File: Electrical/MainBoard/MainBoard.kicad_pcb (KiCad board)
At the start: 4 copper layers, 0 parts

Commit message: Add the majority of the electronics
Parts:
- added C1: 0.1 uF, Capacitor_SMD:C_0805_2012Metric_Pad1.18x1.45mm_HandSolder, F.Cu at (238.4, 136.1)
- added C10: 0.1 uF, Capacitor_SMD:C_0805_2012Metric_Pad1.18x1.45mm_HandSolder, F.Cu at (243.2, 148.1)
- added C11: 4.7 uF, Capacitor_SMD:C_0805_2012Metric_Pad1.18x1.45mm_HandSolder, F.Cu at (203.9, 170.2)
- added C12: 4.7 uF, Capacitor_SMD:C_0805_2012Metric_Pad1.18x1.45mm_HandSolder, F.Cu at (203.9, 173.2)
- added C13: 10 uF, Capacitor_THT:CP_Radial_Tantal_D5.0mm_P2.50mm, F.Cu at (197.0, 172.0)
- added C14: 0.1 uF, Capacitor_SMD:C_0805_2012Metric_Pad1.18x1.45mm_HandSolder, F.Cu at (204.2, 103.0)
- added C15: 2.2 uF, Capacitor_SMD:C_0805_2012Metric_Pad1.18x1.45mm_HandSolder, F.Cu at (204.2, 106.0)
- added C16: 10 nF, Capacitor_SMD:C_0805_2012Metric_Pad1.18x1.45mm_HandSolder, F.Cu at (204.2, 109.0)
- added C17: 0.1 uF, Capacitor_SMD:C_0805_2012Metric_Pad1.18x1.45mm_HandSolder, F.Cu at (192.0, 98.0)
- added C18: 4.7 uF, Capacitor_SMD:C_0805_2012Metric_Pad1.18x1.45mm_HandSolder, F.Cu at (267.4, 143.5)
- added C19: 4.7 uF, Capacitor_SMD:C_0805_2012Metric_Pad1.18x1.45mm_HandSolder, F.Cu at (267.4, 146.5)
- added C2: 0.1 uF, Capacitor_SMD:C_0805_2012Metric_Pad1.18x1.45mm_HandSolder, F.Cu at (238.4, 139.1)
- added C3: 0.1 uF, Capacitor_SMD:C_0805_2012Metric_Pad1.18x1.45mm_HandSolder, F.Cu at (238.4, 142.1)
- added C4: 0.1 uF, Capacitor_SMD:C_0805_2012Metric_Pad1.18x1.45mm_HandSolder, F.Cu at (238.4, 145.1)
- added C5: 0.1 uF, Capacitor_SMD:C_0805_2012Metric_Pad1.18x1.45mm_HandSolder, F.Cu at (238.4, 148.1)
- added C6: 0.1 uF, Capacitor_SMD:C_0805_2012Metric_Pad1.18x1.45mm_HandSolder, F.Cu at (243.2, 136.1)
- added C7: 0.1 uF, Capacitor_SMD:C_0805_2012Metric_Pad1.18x1.45mm_HandSolder, F.Cu at (243.2, 139.1)
- added C8: 0.1 uF, Capacitor_SMD:C_0805_2012Metric_Pad1.18x1.45mm_HandSolder, F.Cu at (243.2, 142.1)
- added C9: 0.1 uF, Capacitor_SMD:C_0805_2012Metric_Pad1.18x1.45mm_HandSolder, F.Cu at (243.2, 145.1)
- added D1: LED 2, LED_SMD:LED_0805_2012Metric_Pad1.15x1.40mm_HandSolder, F.Cu at (197.3, 150.0)
- added D2: LED 1, LED_SMD:LED_0805_2012Metric_Pad1.15x1.40mm_HandSolder, F.Cu at (197.3, 153.0)
- added D3: LED 4, LED_SMD:LED_0805_2012Metric_Pad1.15x1.40mm_HandSolder, F.Cu at (197.3, 156.1)
- added D4: LED 3, LED_SMD:LED_0805_2012Metric_Pad1.15x1.40mm_HandSolder, F.Cu at (197.3, 159.1)
- added D5: LED 6, LED_SMD:LED_0805_2012Metric_Pad1.15x1.40mm_HandSolder, F.Cu at (197.3, 162.2)
- added D6: LED 5, LED_SMD:LED_0805_2012Metric_Pad1.15x1.40mm_HandSolder, F.Cu at (197.3, 165.2)
- added D7: ON, LED_SMD:LED_0805_2012Metric_Pad1.15x1.40mm_HandSolder, F.Cu at (203.9, 176.3)
- added D8: Status_LED, RobotLibrary:CONN3_22232031_MOL, F.Cu at (192.7, 105.4)
- added F1: 5A Fuse, RobotLibrary:FUSE_4628, F.Cu at (228.3, 75.0)
- added H1: MountingHole, MountingHole:MountingHole_3.2mm_M3, F.Cu at (169.2, 86.0)
- added H2: MountingHole, MountingHole:MountingHole_3.2mm_M3, F.Cu at (261.7, 86.0)
- added H3: MountingHole, MountingHole:MountingHole_3.2mm_M3, F.Cu at (169.3, 178.5)
- added H4: MountingHole, MountingHole:MountingHole_3.2mm_M3, F.Cu at (261.7, 178.5)
- added J1: SNAP Program, Connector_PinSocket_2.54mm:PinSocket_1x06_P2.54mm_Horizontal, F.Cu at (247.0, 116.6)
- added J10: Refl_Mount, Connector_PinHeader_2.54mm:PinHeader_2x02_P2.54mm_Vertical, F.Cu at (250.2, 196.1)
- added J11: Refl_Mount, Connector_PinHeader_2.54mm:PinHeader_2x02_P2.54mm_Vertical, F.Cu at (250.2, 203.3)
- added J12: Refl_PCB_Connect, RobotLibrary:CONN3_22232031_MOL, F.Cu at (255.6, 96.7)
- added J13: Refl_PCB_Connect, RobotLibrary:CONN3_22232031_MOL, F.Cu at (255.6, 104.7)
- added J14: Refl_PCB_Connect, RobotLibrary:CONN3_22232031_MOL, F.Cu at (255.6, 112.7)
- added J2: UART Connect, Connector_PinHeader_2.54mm:PinHeader_2x06_P2.54mm_Vertical, F.Cu at (204.9, 122.6)
- added J3: SPI Connect, Connector_PinHeader_2.54mm:PinHeader_2x08_P2.54mm_Vertical, F.Cu at (197.7, 122.6)
- added J4: 5V Supply, Connector_PinHeader_2.54mm:PinHeader_2x05_P2.54mm_Vertical, F.Cu at (250.8, 155.8)
- added J5: 3.3V Supply, Connector_PinHeader_2.54mm:PinHeader_2x05_P2.54mm_Vertical, F.Cu at (258.0, 155.8)
- added J6: USB_B_Micro, RobotLibrary:AMPHENOL_10118193-0001LF, F.Cu at (217.5, 110.4)
- added J7: Battery1, RobotLibrary:CONN_1017514, F.Cu at (218.2, 86.7)
- added J8: Battery1, RobotLibrary:CONN_1017514, F.Cu at (234.8, 86.7)
- added J9: Refl_Mount, Connector_PinHeader_2.54mm:PinHeader_2x02_P2.54mm_Vertical, F.Cu at (239.8, 187.7)
- added K1: QRE1113GR, RobotLibrary:ARUSM-313_100CY_FAS-M, F.Cu at (234.6, 189.4)
- added K2: QRE1113GR, RobotLibrary:ARUSM-313_100CY_FAS-M, F.Cu at (250.7, 189.7)
- added K3: QRE1113GR, RobotLibrary:ARUSM-313_100CY_FAS-M, F.Cu at (256.5, 189.7)
- added R1: 1k, Resistor_SMD:R_0805_2012Metric_Pad1.20x1.40mm_HandSolder, F.Cu at (222.8, 144.0)
- added R10: 1k, Resistor_SMD:R_0805_2012Metric_Pad1.20x1.40mm_HandSolder, F.Cu at (190.5, 150.0)
- added R11: 1k, Resistor_SMD:R_0805_2012Metric_Pad1.20x1.40mm_HandSolder, F.Cu at (190.5, 152.9)
- added R12: 1k, Resistor_SMD:R_0805_2012Metric_Pad1.20x1.40mm_HandSolder, F.Cu at (190.5, 155.9)
- added R13: 1k, Resistor_SMD:R_0805_2012Metric_Pad1.20x1.40mm_HandSolder, F.Cu at (190.5, 158.8)
- added R14: 1k, Resistor_SMD:R_0805_2012Metric_Pad1.20x1.40mm_HandSolder, F.Cu at (185.2, 86.3)
- added R15: 1k, Resistor_SMD:R_0805_2012Metric_Pad1.20x1.40mm_HandSolder, F.Cu at (185.2, 89.2)
- added R16: 1k, Resistor_SMD:R_0805_2012Metric_Pad1.20x1.40mm_HandSolder, F.Cu at (185.2, 92.2)
- added R17: 130R, Resistor_SMD:R_0805_2012Metric_Pad1.20x1.40mm_HandSolder, F.Cu at (191.9, 111.0)
- added R18: 130R, Resistor_SMD:R_0805_2012Metric_Pad1.20x1.40mm_HandSolder, F.Cu at (191.9, 113.9)
- added R19: 100R, Resistor_SMD:R_0805_2012Metric_Pad1.20x1.40mm_HandSolder, F.Cu at (239.9, 194.1)
- added R2: 10k, Resistor_SMD:R_0805_2012Metric_Pad1.20x1.40mm_HandSolder, F.Cu at (222.8, 147.0)
- added R20: 10k, Resistor_SMD:R_0805_2012Metric_Pad1.20x1.40mm_HandSolder, F.Cu at (239.9, 197.0)
- added R21: 100R, Resistor_SMD:R_0805_2012Metric_Pad1.20x1.40mm_HandSolder, F.Cu at (257.4, 195.2)
- added R22: 10k, Resistor_SMD:R_0805_2012Metric_Pad1.20x1.40mm_HandSolder, F.Cu at (257.4, 198.2)
- added R23: 100R, Resistor_SMD:R_0805_2012Metric_Pad1.20x1.40mm_HandSolder, F.Cu at (257.4, 201.2)
- added R24: 10k, Resistor_SMD:R_0805_2012Metric_Pad1.20x1.40mm_HandSolder, F.Cu at (257.4, 204.1)
- added R3: 130R, Resistor_SMD:R_0805_2012Metric_Pad1.20x1.40mm_HandSolder, F.Cu at (202.0, 150.0)
- added R4: 130R, Resistor_SMD:R_0805_2012Metric_Pad1.20x1.40mm_HandSolder, F.Cu at (202.0, 152.9)
- added R5: 130R, Resistor_SMD:R_0805_2012Metric_Pad1.20x1.40mm_HandSolder, F.Cu at (202.0, 155.9)
- added R6: 130R, Resistor_SMD:R_0805_2012Metric_Pad1.20x1.40mm_HandSolder, F.Cu at (202.0, 158.8)
- added R7: 130R, Resistor_SMD:R_0805_2012Metric_Pad1.20x1.40mm_HandSolder, F.Cu at (202.0, 161.8)
- added R8: 130R, Resistor_SMD:R_0805_2012Metric_Pad1.20x1.40mm_HandSolder, F.Cu at (202.0, 164.7)
- added R9: 130R, Resistor_SMD:R_0805_2012Metric_Pad1.20x1.40mm_HandSolder, F.Cu at (197.2, 176.7)
- added SW1: Reset, RobotLibrary:SW_B3F-1000_OMR, F.Cu at (212.3, 145.8)
- added SW10: User_Button, RobotLibrary:CONN_22232021_MOL, F.Cu at (178.3, 104.8)
- added SW2: 5V Bypass, RobotLibrary:SPDT_OS102011_CNK, F.Cu at (209.3, 87.5)
- added SW3: All Power Switch, RobotLibrary:26-60-4040_MOL, F.Cu at (189.4, 74.4)
- added SW4: SW_SPST, RobotLibrary:CONN_22232021_MOL, F.Cu at (183.5, 152.4)
- added SW5: SW_SPST, RobotLibrary:CONN_22232021_MOL, F.Cu at (183.5, 160.4)
- added SW6: SW_SPST, RobotLibrary:CONN_22232021_MOL, F.Cu at (183.5, 168.4)
- added SW7: SW_SPST, RobotLibrary:CONN_22232021_MOL, F.Cu at (183.5, 176.4)
- added SW8: User_Button, RobotLibrary:CONN_22232021_MOL, F.Cu at (178.3, 88.7)
- added SW9: User_Button, RobotLibrary:CONN_22232021_MOL, F.Cu at (178.3, 96.8)
- added U1: PIC32MZ2048EFH144-I/PL, RobotLibrary:LQFP144_PL_MCH-M, F.Cu at (223.4, 129.9)
- added U2: GSF7002DW, Package_TO_SOT_SMD:SOT-363_SC-70-6, F.Cu at (206.5, 150.4)
- added U3: GSF7002DW, Package_TO_SOT_SMD:SOT-363_SC-70-6, F.Cu at (206.5, 154.3)
- added U4: GSF7002DW, Package_TO_SOT_SMD:SOT-363_SC-70-6, F.Cu at (206.5, 158.1)
- added U5: AP2114HA-3.3TRG1, RobotLibrary:SOT-223_DIO-M, F.Cu at (180.6, 122.7)
- added U6: ICM-42688-P, RobotLibrary:LGA14_2P5X3X0P91_TDK-M, F.Cu at (210.9, 171.0)
- added U7: MAX-M8C-0, RobotLibrary:XCVR_MAX-M8C-0, F.Cu at (197.2, 90.6)
- added U8: GSF7002DW, Package_TO_SOT_SMD:SOT-363_SC-70-6, F.Cu at (196.4, 111.4)
- added U9: AP2114HA-3.3TRG1, RobotLibrary:SOT-223_DIO-M, F.Cu at (260.9, 146.9)
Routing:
- added copper zone on In2.Cu, net +3.3V
- added copper zone on In1.Cu, net GND
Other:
- board outline added: 100 x 100 mm
- board text added: "2"
- board text added: "3"

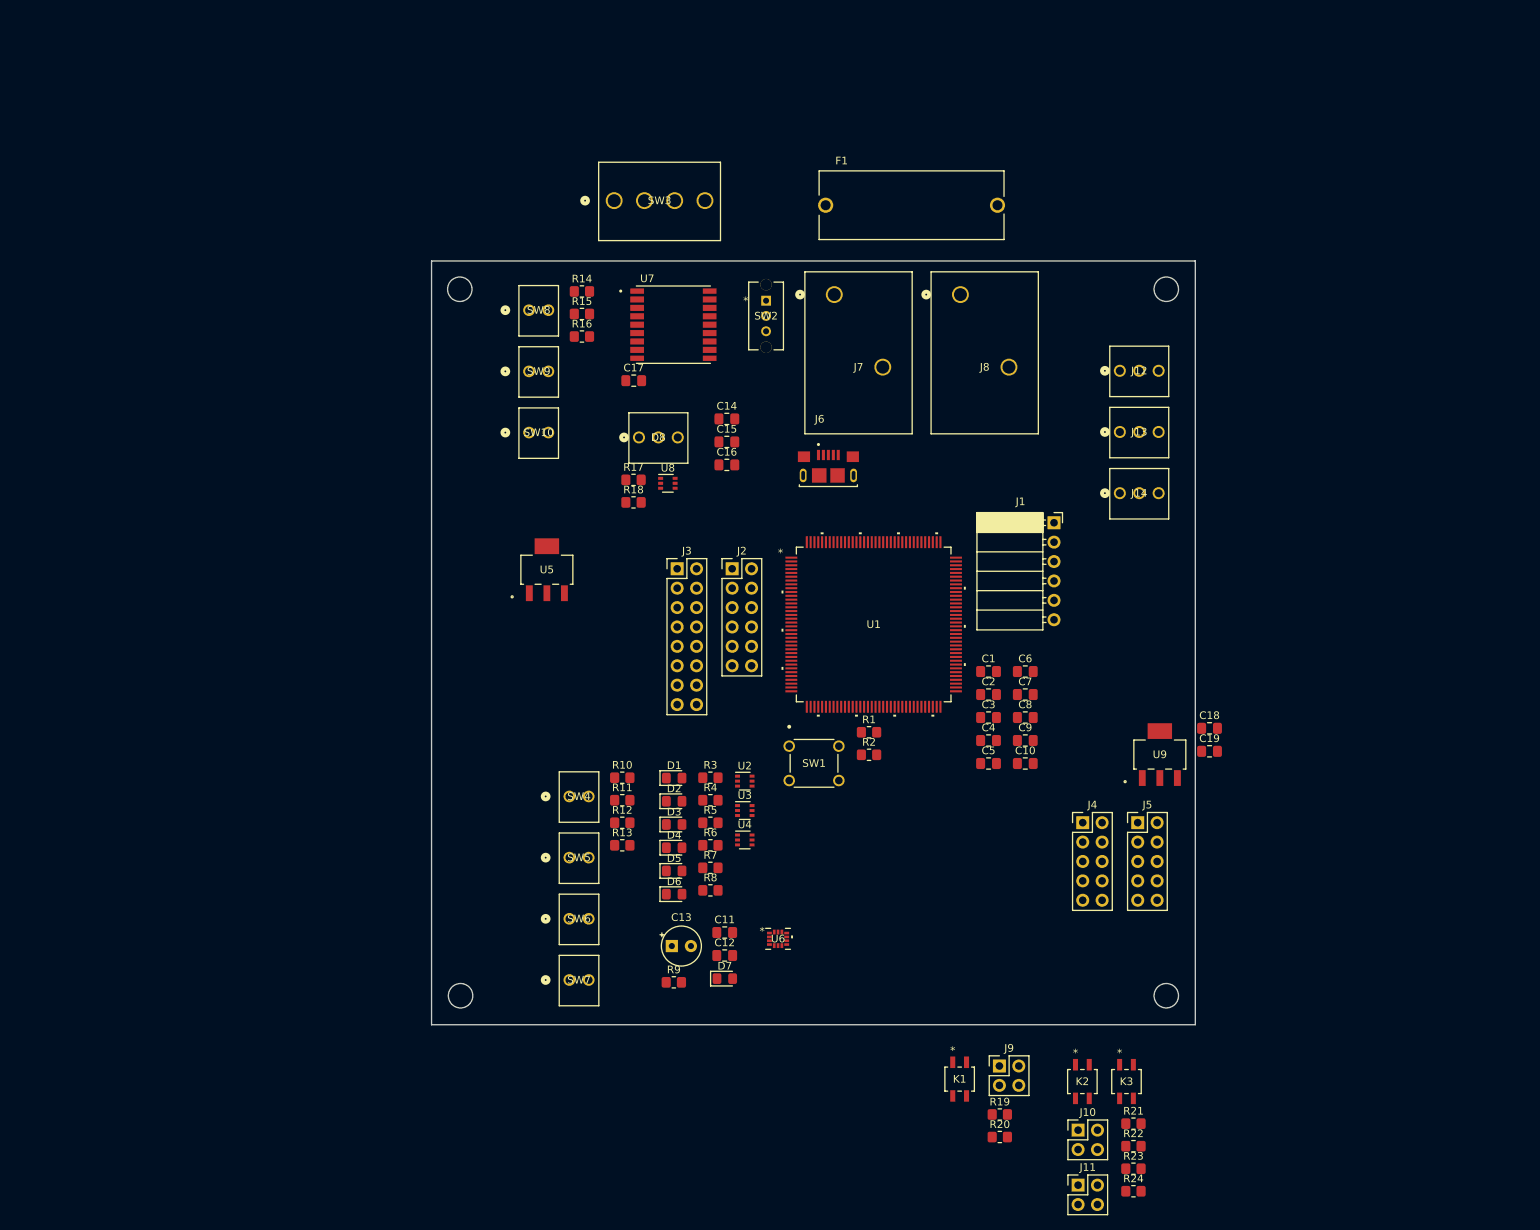
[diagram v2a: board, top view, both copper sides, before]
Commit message: Add more schematics and begin floorplanning
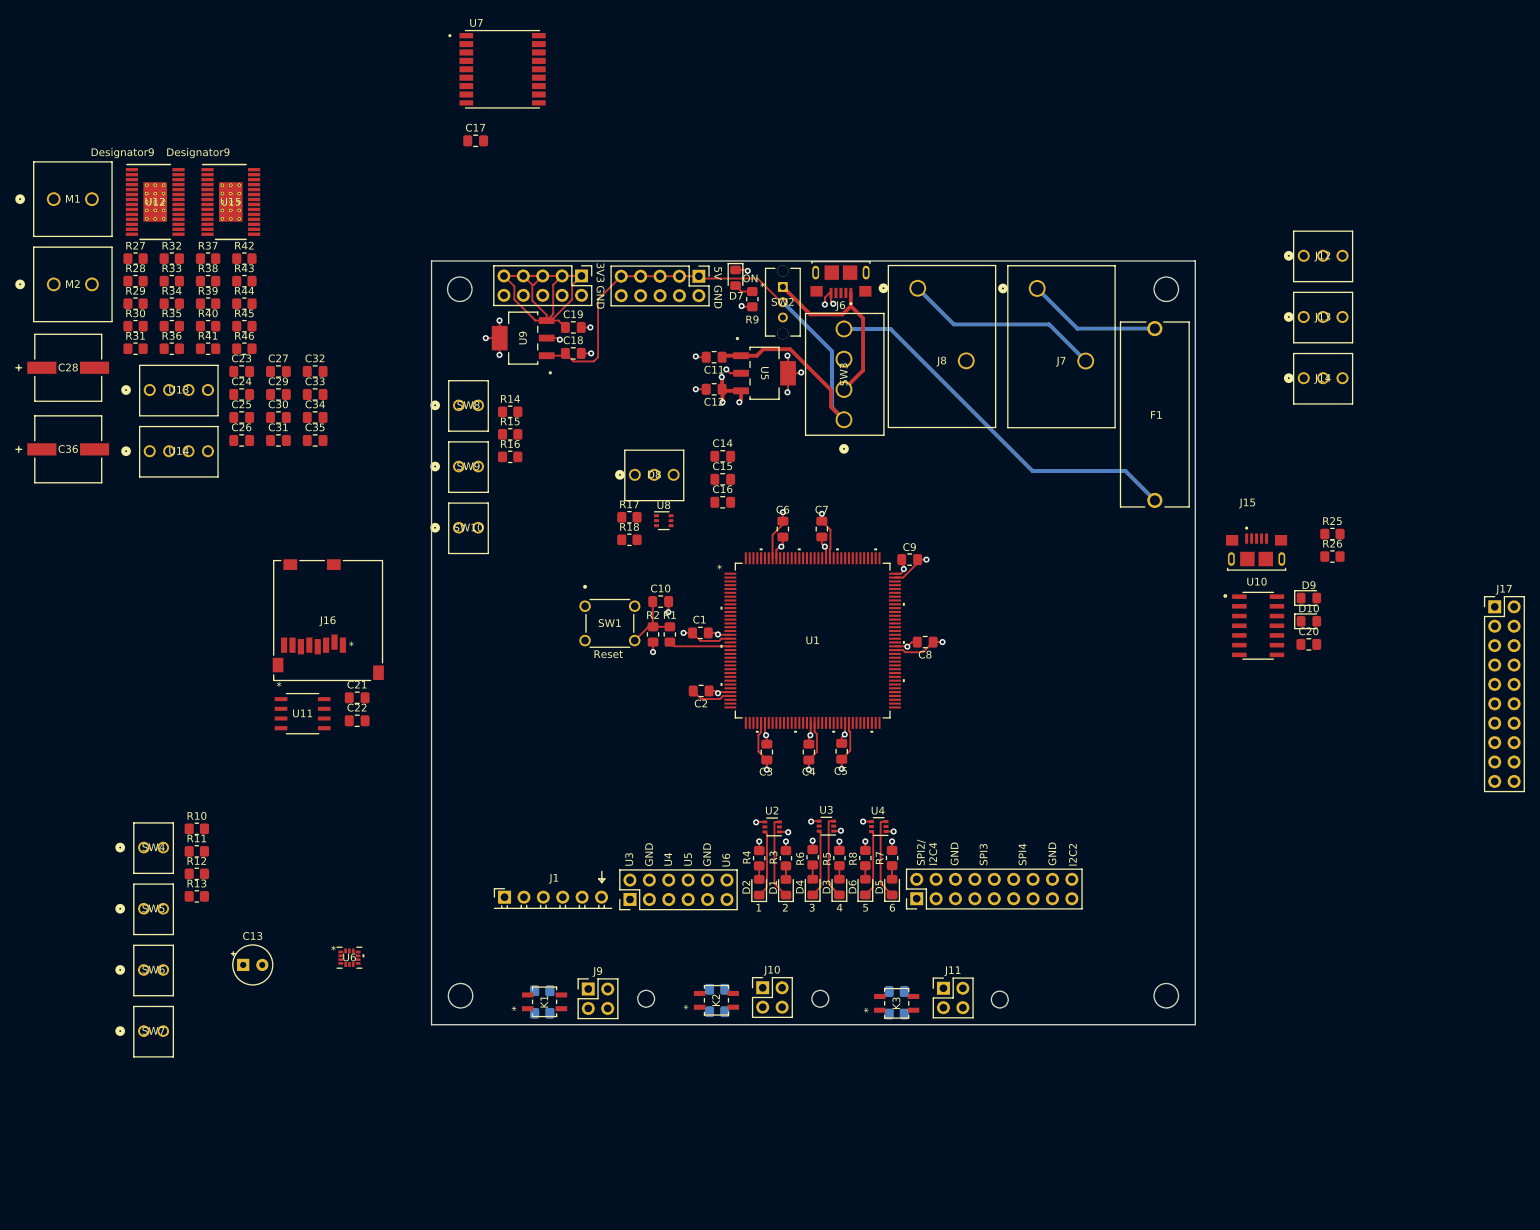
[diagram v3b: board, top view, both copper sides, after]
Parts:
- added C20: 0.1 uF, Capacitor_SMD:C_0805_2012Metric_Pad1.18x1.45mm_HandSolder, F.Cu at (280.4, 132.5)
- added C21: 0.1 uF, Capacitor_SMD:C_0805_2012Metric_Pad1.18x1.45mm_HandSolder, F.Cu at (155.8, 139.5)
- added C22: 0.1 uF, Capacitor_SMD:C_0805_2012Metric_Pad1.18x1.45mm_HandSolder, F.Cu at (155.8, 142.5)
- added C23: 0.47 uF, Capacitor_SMD:C_0805_2012Metric_Pad1.18x1.45mm_HandSolder, F.Cu at (140.6, 96.8)
- added C24: 0.01 uF, Capacitor_SMD:C_0805_2012Metric_Pad1.18x1.45mm_HandSolder, F.Cu at (140.6, 99.8)
- added C25: 0.1 uF, Capacitor_SMD:C_0805_2012Metric_Pad1.18x1.45mm_HandSolder, F.Cu at (140.6, 102.8)
- added C26: 0.1 uF, Capacitor_SMD:C_0805_2012Metric_Pad1.18x1.45mm_HandSolder, F.Cu at (140.6, 105.8)
- added C27: 0.1 uF, Capacitor_SMD:C_0805_2012Metric_Pad1.18x1.45mm_HandSolder, F.Cu at (145.5, 96.8)
- added C28: 100 uF, RobotLibrary:PCAP_8x10-ELECT_NCA-M, F.Cu at (117.9, 96.3)
- added C29: 0.1 uF, Capacitor_SMD:C_0805_2012Metric_Pad1.18x1.45mm_HandSolder, F.Cu at (145.5, 99.8)
- added C30: 0.1 uF, Capacitor_SMD:C_0805_2012Metric_Pad1.18x1.45mm_HandSolder, F.Cu at (145.5, 102.8)
- added C31: 0.47 uF, Capacitor_SMD:C_0805_2012Metric_Pad1.18x1.45mm_HandSolder, F.Cu at (145.5, 105.8)
- added C32: 0.01 uF, Capacitor_SMD:C_0805_2012Metric_Pad1.18x1.45mm_HandSolder, F.Cu at (150.3, 96.8)
- added C33: 0.1 uF, Capacitor_SMD:C_0805_2012Metric_Pad1.18x1.45mm_HandSolder, F.Cu at (150.3, 99.8)
- added C34: 0.1 uF, Capacitor_SMD:C_0805_2012Metric_Pad1.18x1.45mm_HandSolder, F.Cu at (150.3, 102.8)
- added C35: 0.1 uF, Capacitor_SMD:C_0805_2012Metric_Pad1.18x1.45mm_HandSolder, F.Cu at (150.3, 105.8)
- added C36: 100 uF, RobotLibrary:PCAP_8x10-ELECT_NCA-M, F.Cu at (117.9, 107.0)
- added D10: LED, LED_SMD:LED_0805_2012Metric_Pad1.15x1.40mm_HandSolder, F.Cu at (280.4, 129.5)
- added D9: LED, LED_SMD:LED_0805_2012Metric_Pad1.15x1.40mm_HandSolder, F.Cu at (280.4, 126.4)
- added H5: MountingHole, MountingHole:MountingHole_2.2mm_M2, F.Cu at (193.6, 178.9)
- added H6: MountingHole, MountingHole:MountingHole_2.2mm_M2, F.Cu at (216.4, 178.9)
- added H7: MountingHole, MountingHole:MountingHole_2.2mm_M2, F.Cu at (239.9, 179.0)
- added J15: USB_B_Micro, RobotLibrary:AMPHENOL_10118193-0001LF, F.Cu at (273.5, 121.3)
- added J16: MEM2061-01-188-00-A, RobotLibrary:MEM2061-01-188-00-A_GCT, F.Cu at (152.0, 129.4)
- added J17: GPIO, Connector_PinHeader_2.54mm:PinHeader_2x10_P2.54mm_Vertical, F.Cu at (304.7, 127.6)
- added M1: Motor_DC, RobotLibrary:CONN_1890963_PXC, F.Cu at (116.0, 74.2)
- added M2: Motor_DC, RobotLibrary:CONN_1890963_PXC, F.Cu at (116.0, 85.4)
- added R25: 130R, Resistor_SMD:R_0805_2012Metric_Pad1.20x1.40mm_HandSolder, F.Cu at (283.5, 118.0)
- added R26: 130R, Resistor_SMD:R_0805_2012Metric_Pad1.20x1.40mm_HandSolder, F.Cu at (283.5, 121.0)
- added R27: 10k, Resistor_SMD:R_0805_2012Metric_Pad1.20x1.40mm_HandSolder, F.Cu at (126.7, 82.0)
- added R28: 16k, Resistor_SMD:R_0805_2012Metric_Pad1.20x1.40mm_HandSolder, F.Cu at (126.7, 84.9)
- added R29: 51k, Resistor_SMD:R_0805_2012Metric_Pad1.20x1.40mm_HandSolder, F.Cu at (126.7, 87.9)
- added R30: 0R, Resistor_SMD:R_0805_2012Metric_Pad1.20x1.40mm_HandSolder, F.Cu at (126.7, 90.8)
- added R31: 0R, Resistor_SMD:R_0805_2012Metric_Pad1.20x1.40mm_HandSolder, F.Cu at (126.7, 93.8)
- added R32: 0R, Resistor_SMD:R_0805_2012Metric_Pad1.20x1.40mm_HandSolder, F.Cu at (131.5, 82.0)
- added R33: 0R, Resistor_SMD:R_0805_2012Metric_Pad1.20x1.40mm_HandSolder, F.Cu at (131.5, 84.9)
- added R34: 0R, Resistor_SMD:R_0805_2012Metric_Pad1.20x1.40mm_HandSolder, F.Cu at (131.5, 87.9)
- added R35: 1M, Resistor_SMD:R_0805_2012Metric_Pad1.20x1.40mm_HandSolder, F.Cu at (131.5, 90.8)
- added R36: 0.25R, Resistor_SMD:R_0805_2012Metric_Pad1.20x1.40mm_HandSolder, F.Cu at (131.5, 93.8)
- added R37: 10k, Resistor_SMD:R_0805_2012Metric_Pad1.20x1.40mm_HandSolder, F.Cu at (136.2, 82.0)
- added R38: 16k, Resistor_SMD:R_0805_2012Metric_Pad1.20x1.40mm_HandSolder, F.Cu at (136.2, 84.9)
- added R39: 51k, Resistor_SMD:R_0805_2012Metric_Pad1.20x1.40mm_HandSolder, F.Cu at (136.2, 87.9)
- added R40: 0R, Resistor_SMD:R_0805_2012Metric_Pad1.20x1.40mm_HandSolder, F.Cu at (136.2, 90.8)
- added R41: 0R, Resistor_SMD:R_0805_2012Metric_Pad1.20x1.40mm_HandSolder, F.Cu at (136.2, 93.8)
- added R42: 0R, Resistor_SMD:R_0805_2012Metric_Pad1.20x1.40mm_HandSolder, F.Cu at (141.0, 82.0)
- added R43: 0R, Resistor_SMD:R_0805_2012Metric_Pad1.20x1.40mm_HandSolder, F.Cu at (141.0, 84.9)
- added R44: 0R, Resistor_SMD:R_0805_2012Metric_Pad1.20x1.40mm_HandSolder, F.Cu at (141.0, 87.9)
- added R45: 1M, Resistor_SMD:R_0805_2012Metric_Pad1.20x1.40mm_HandSolder, F.Cu at (141.0, 90.8)
- added R46: 0.25R, Resistor_SMD:R_0805_2012Metric_Pad1.20x1.40mm_HandSolder, F.Cu at (141.0, 93.8)
- added U10: MCP2221A-I_SL, RobotLibrary:SOIC127P600X175-14N, F.Cu at (273.7, 130.1)
- added U11: M95M01-DFMN6TP, RobotLibrary:SO8N_4X5X1P27_STM-M, F.Cu at (148.6, 141.6)
- added U12: DRV8842PWPR, RobotLibrary:PWP0028C_M, F.Cu at (129.3, 74.6)
- added U13: Quad_Encoder, RobotLibrary:CONN_22-23-2041_MOL, F.Cu at (128.6, 99.2)
- added U14: Quad_Encoder, RobotLibrary:CONN_22-23-2041_MOL, F.Cu at (128.6, 107.2)
- added U15: DRV8842PWPR, RobotLibrary:PWP0028C_M, F.Cu at (139.2, 74.6)
- J3: value SPI Connect -> SPI/I2C Connect; footprint Connector_PinHeader_2.54mm:PinHeader_2x08_P2.54mm_Vertical -> Connector_PinHeader_2.54mm:PinHeader_2x09_P2.54mm_Vertical
- R19, R20, R21, R22, R23, R24: moved to B.Cu
- moved J5 102.1 mm to (185.1, 84.3), turned to -90 degrees
- moved C19 100.1 mm to (184.1, 91.0)
- moved U9 99.6 mm to (177.5, 92.4), turned to 90 degrees
- moved C18 96.7 mm to (184.1, 94.4)
- moved D7 91.8 mm to (205.3, 84.5), turned to -90 degrees
- moved R9 90.0 mm to (207.5, 87.3), turned to 90 degrees
- moved J4 87.4 mm to (200.5, 84.3), turned to -90 degrees
- moved J1 87.1 mm to (175.1, 165.6), turned to 90 degrees
- moved C11 75.3 mm to (202.5, 94.9), turned to 180 degrees
- moved C12 74.1 mm to (202.5, 99.1), turned to 180 degrees
- moved R19 62.1 mm to (180.0, 177.8), turned to 180 degrees
- moved R20 62.1 mm to (180.0, 180.8), turned to 180 degrees
- moved R21 57.3 mm to (202.9, 177.7), turned to 180 degrees
- moved R22 57.3 mm to (202.9, 180.6), turned to 180 degrees
- moved C13 56.2 mm to (140.8, 174.5)
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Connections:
- D6 pad 1: Net-(D6-K) -> unconnected-(D6-K-Pad1)
- J2 pad 1: /U1TX -> /U3TX
- J2 pad 10: /U5RX -> GND
- J2 pad 2: /U1RX -> /U3RX
- J2 pad 3: unconnected-(J2-Pin_3-Pad3) -> GND
- J2 pad 4: unconnected-(J2-Pin_4-Pad4) -> GND
- J2 pad 5: /U3TX -> /U4TX
- J2 pad 6: /U3RX -> /U4RX
- J2 pad 7: /U4TX -> /U5TX
- J2 pad 8: /U4RX -> /U5RX
- J2 pad 9: /U5TX -> GND
- J3 pad 1: /SCK3 -> /SCK2
- J3 pad 10: /SDO5 -> /SDI3
- J3 pad 11: /SS5* -> /SCK4
- J3 pad 12: /SDI5 -> /SDO4
- J3 pad 13: /SCK6 -> /SS4*
- J3 pad 14: /SDO6 -> /SDI4
- J3 pad 15: /SS6* -> GND
- J3 pad 16: /SDI6 -> GND
- J3 pad 2: /SDO3 -> /SDO2
- J3 pad 3: /SS3* -> /SS2*
- J3 pad 4: /SDI3 -> /SDI2
- J3 pad 5: /SCK4 -> GND
- J3 pad 6: /SDO4 -> GND
- J3 pad 7: /SS4* -> /SCK3
- J3 pad 8: /SDI4 -> /SDO3
- J3 pad 9: /SCK5 -> /SS3*
- U1 pad 10: unconnected-(U1A-EBIBS1/RJ10-Pad10) -> /Fault2
- U1 pad 100: unconnected-(U1B-ECRS/RH12-Pad100) -> /RH12
- U1 pad 101: unconnected-(U1B-ERXDV/ECRSDV/RH13-Pad101) -> /RH13
- U1 pad 102: unconnected-(U1B-RH14-Pad102) -> /RH14
- U1 pad 103: unconnected-(U1B-EBIA23/RH15-Pad103) -> /RH15
- U1 pad 117: unconnected-(U1B-EBIA22/RJ3-Pad117) -> /Dir2
- U1 pad 26: unconnected-(U1A-AN4/C1INB/RB4-Pad26) -> /RB4
- U1 pad 27: unconnected-(U1A-AN37/ERXCLK/EREFCLK/RJ11-Pad27) -> /RJ11
- U1 pad 28: unconnected-(U1A-EBIA13/PMA13/RJ13-Pad28) -> /RJ13
- U1 pad 29: unconnected-(U1A-EBIA11/PMA11/RJ14-Pad29) -> /RJ14
- U1 pad 30: unconnected-(U1A-EBIA0/PMA0/RJ15-Pad30) -> /RJ15
- U1 pad 39: unconnected-(U1A-VREF-/CVREF-/AN27/RA9-Pad39) -> /RA9
- U1 pad 40: unconnected-(U1A-VREF+/CVREF+/AN28/RA10-Pad40) -> /RA10
- U1 pad 43: unconnected-(U1A-AN38/ETXD2/RH0-Pad43) -> /RH0
- U1 pad 44: unconnected-(U1A-AN39/ETXD3/RH1-Pad44) -> /RH1
- U1 pad 45: unconnected-(U1A-EBIRP/RH2-Pad45) -> /RH2
- U1 pad 46: unconnected-(U1A-RH3-Pad46) -> /RH3
- U1 pad 49: unconnected-(U1A-CVREFOUT/AN5/RPB10/RB10-Pad49) -> /RB10
- U1 pad 50: unconnected-(U1A-AN6/RB11-Pad50) -> /RB11
- U1 pad 51: unconnected-(U1A-EBIA1/PMA1/RK1-Pad51) -> /RK1
- U1 pad 52: unconnected-(U1A-EBIA3/PMA3/RK2-Pad52) -> /RK2
- U1 pad 53: unconnected-(U1A-EBIA17/RK3-Pad53) -> /RK3
- U1 pad 56: unconnected-(U1A-TCK/AN29/RA1-Pad56) -> /MotorCurrent2
- U1 pad 59: unconnected-(U1A-AN7/RB12-Pad59) -> /Write Protect*
- U1 pad 60: unconnected-(U1A-AN8/RB13-Pad60) -> /Hold*
- U1 pad 74: unconnected-(U1B-VUSB3V3-Pad74) -> GND
- U1 pad 8: unconnected-(U1A-AN36/ETXD1/RJ9-Pad8) -> /MotorCurrent1
- U1 pad 80: unconnected-(U1B-SCL3/RPF8/RF8-Pad80) -> /Dir1
- U1 pad 85: unconnected-(U1B-SCL2/RA2-Pad85) -> /SCL2
- U1 pad 86: unconnected-(U1B-EBIRDY1/SDA2/RA3-Pad86) -> /SDA2
- U1 pad 9: unconnected-(U1A-EBIBS0/RJ12-Pad9) -> /Fault1
- U1 pad 92: unconnected-(U1B-EBIA18/RK4-Pad92) -> /USB_RST
- U4 pad 1: GND -> unconnected-(U4-S1-Pad1)
- U4 pad 2: /LED2 -> unconnected-(U4-G1-Pad2)
- U4 pad 3: Net-(D5-K) -> unconnected-(U4-D2-Pad3)
- U4 pad 4: GND -> Net-(D5-K)
- U4 pad 5: /LED1 -> /LED2
- U4 pad 6: Net-(D6-K) -> unconnected-(U4-D1-Pad6)
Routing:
- net +5V: track 0.00 -> 82.1 mm
- net +3.3V: track 0.00 -> 74.8 mm, vias 0 -> 19
- net GND: track 0.00 -> 60.1 mm, vias 0 -> 29
- net Net-(F1-Pad1): track 0.00 -> 50.0 mm
- net Net-(J5-Pin_1): track 0.00 -> 45.7 mm
- net Net-(J7-Pin_2): track 0.00 -> 25.9 mm
- net Net-(J6-VBUS): track 0.00 -> 25.2 mm
- net Net-(J7-Pin_1): track 0.00 -> 17.6 mm
- net Net-(D5-K): track 0.00 -> 11.9 mm, vias 0 -> 1
- net Net-(D3-K): track 0.00 -> 10.8 mm
- net Net-(D1-K): track 0.00 -> 10.8 mm
- net Net-(D4-K): track 0.00 -> 8.85 mm
- net (no net): track 0.00 -> 8.82 mm
- net Net-(D2-K): track 0.00 -> 8.81 mm
- net Net-(C10-Pad1): track 0.00 -> 8.66 mm
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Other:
- board text added: "1"
- board text added: "3V3"
- board text added: "4"
- board text added: "5"
- board text added: "5V"
- board text added: "6"
- board text added: "GND"
- board text added: "I2C2"
- board text added: "ON"
- board text added: "Reset"
- board text added: "SPI2/ I2C4"
- board text added: "SPI3"
- board text added: "SPI4"
- board text added: "U3"
- board text added: "U4"
- board text added: "U5"
- board text added: "U6"
